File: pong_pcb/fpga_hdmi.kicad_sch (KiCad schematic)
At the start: 13 parts, among them J11 Conn_01x08_Socket, J2 685119134923, J9 Conn_01x14_Socket, U3 TPD12S016RKTR

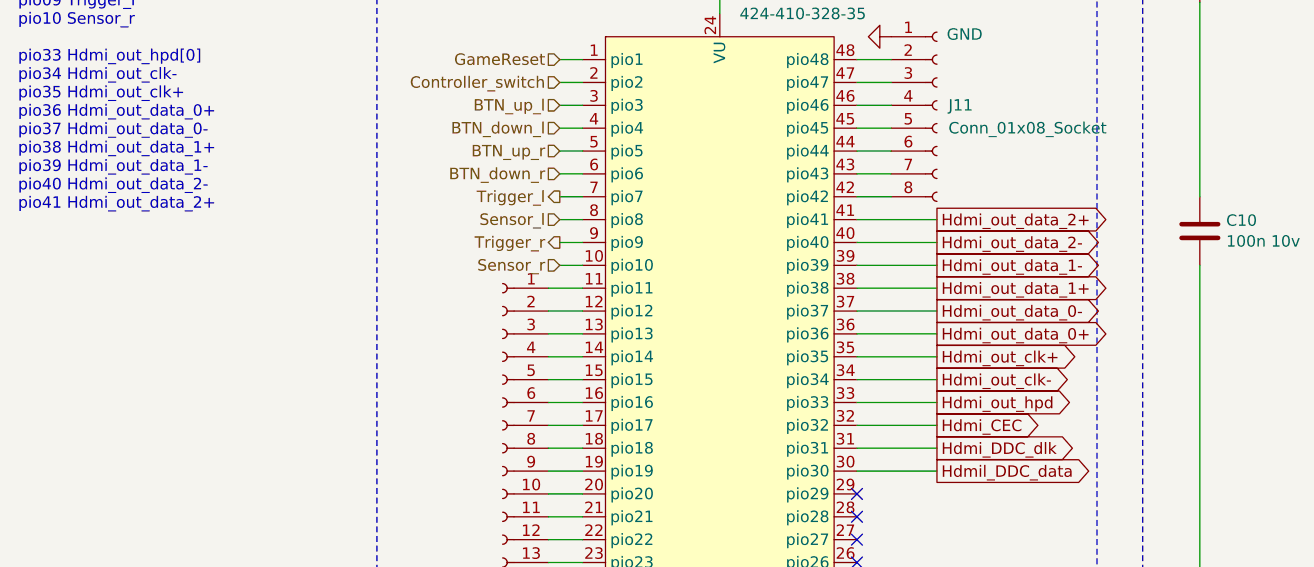
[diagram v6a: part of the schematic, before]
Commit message: Fix HDMI pinout
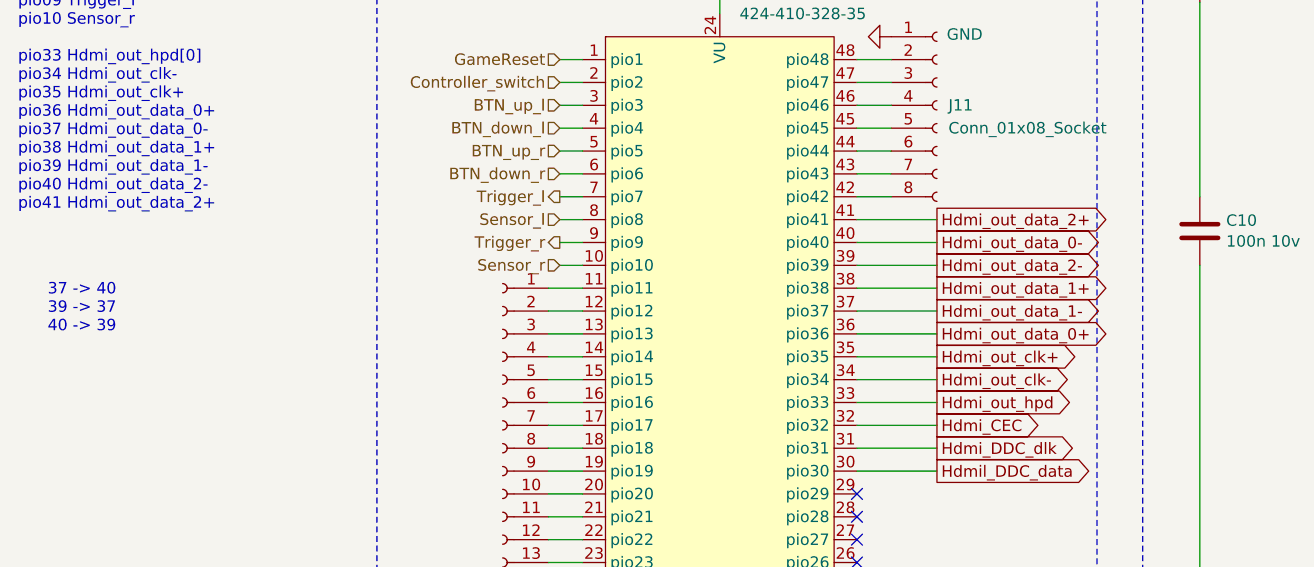
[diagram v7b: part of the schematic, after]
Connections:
- net Hdmi_out_data_0-: now also U2.40 (pio40); no longer U2.37 (pio37)
- net Hdmi_out_data_1-: now also U2.37 (pio37); no longer U2.39 (pio39)
- net Hdmi_out_data_2-: now also U2.39 (pio39); no longer U2.40 (pio40)
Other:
- note added: "37 -> 40 39 -> 37 40 -> 39"
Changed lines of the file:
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@@
+		)
+	)
+	(text "37 -> 40\n39 -> 37\n40 -> 39"
+		(exclude_from_sim no)
+		(at -16.256 70.866 0)
+		(effects
+			(font
+				(size 1.27 1.27)
+			)
 		)
 	)
@@
 	(global_label "Hdmi_out_data_0-"
 		(shape output)
-		(at 78.74 71.12 0)
-		(fields_autoplaced yes)
-		(effects
-			(font
-				(size 1.27 1.27)
-			)
-			(justify left)
-		)
-		(property "Intersheetrefs" "${INTERSHEET_REFS}"
-			(at 100.6539 71.12 0)
+		(at 78.74 63.5 0)
+		(fields_autoplaced yes)
+		(effects
+			(font
+				(size 1.27 1.27)
+			)
+			(justify left)
+		)
+		(property "Intersheetrefs" "${INTERSHEET_REFS}"
+			(at 100.6539 63.5 0)
 			(effects
 				(font
@@
 	(global_label "Hdmi_out_data_1-"
 		(shape output)
-		(at 78.74 66.04 0)
-		(fields_autoplaced yes)
-		(effects
-			(font
-				(size 1.27 1.27)
-			)
-			(justify left)
-		)
-		(property "Intersheetrefs" "${INTERSHEET_REFS}"
-			(at 100.6539 66.04 0)
+		(at 78.74 71.12 0)
+		(fields_autoplaced yes)
+		(effects
+			(font
+				(size 1.27 1.27)
+			)
+			(justify left)
+		)
+		(property "Intersheetrefs" "${INTERSHEET_REFS}"
+			(at 100.6539 71.12 0)
 			(effects
 				(font
@@
 	(global_label "Hdmi_out_data_2-"
 		(shape output)
-		(at 78.74 63.5 0)
-		(fields_autoplaced yes)
-		(effects
-			(font
-				(size 1.27 1.27)
-			)
-			(justify left)
-		)
-		(property "Intersheetrefs" "${INTERSHEET_REFS}"
-			(at 100.6539 63.5 0)
-			(effects
-				(font
+		(at 78.74 66.04 0)
+		(fields_autoplaced yes)
+		(effects
+			(font
+				(size 1.27 1.27)
+			)
+			(justify left)
+		)
+		(property "Intersheetrefs" "${INTERSHEET_REFS}"
+			(at 100.6539 66.04 0)
+			(effects
+				(font
